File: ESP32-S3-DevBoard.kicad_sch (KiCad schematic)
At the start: 27 parts, among them J1 USB_C_Receptacle_USB2.0_14P, J2 Conn_01x22_Socket, J3 Conn_01x22_Socket, SW1 SW_Push, SW2 SW_Push, U1 ESP32-S3-WROOM-1, U2 AMS1117-3.3

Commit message: Add footprints
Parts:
- C1, C2, C3, C4, C5, C6, C7, C8, C9: footprint (none) -> Capacitor_SMD:C_0603_1608Metric_Pad1.08x0.95mm_HandSolder
- D1: footprint (none) -> LED_SMD:LED_0603_1608Metric_Pad1.05x0.95mm_HandSolder
- D2: footprint Diode_THT:D_DO-41_SOD81_P10.16mm_Horizontal -> Diode_SMD:D_SOD-123
- J1: footprint (none) -> Connector_USB:USB_C_Receptacle_GCT_USB4125-xx-x_6P_TopMnt_Horizontal
- J2, J3: footprint (none) -> Connector_PinSocket_2.54mm:PinSocket_1x22_P2.54mm_Vertical
- R1, R2, R3, R4, R5, R6: footprint (none) -> Resistor_SMD:R_0603_1608Metric_Pad0.98x0.95mm_HandSolder
- SW1, SW2: footprint (none) -> Button_Switch_SMD:SW_SPST_PTS810
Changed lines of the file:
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@@
 			)
 		)
-		(property "Footprint" ""
+		(property "Footprint" "Capacitor_SMD:C_0603_1608Metric_Pad1.08x0.95mm_HandSolder"
 			(at 157.7848 91.44 0)
 			(effects
@@
 			)
 		)
-		(property "Footprint" ""
+		(property "Footprint" "Capacitor_SMD:C_0603_1608Metric_Pad1.08x0.95mm_HandSolder"
 			(at 32.7152 40.64 0)
 			(effects
@@
 			)
 		)
-		(property "Footprint" ""
+		(property "Footprint" "Capacitor_SMD:C_0603_1608Metric_Pad1.08x0.95mm_HandSolder"
 			(at 136.8552 49.53 0)
 			(effects
@@
 			)
 		)
-		(property "Footprint" ""
+		(property "Footprint" "Connector_USB:USB_C_Receptacle_GCT_USB4125-xx-x_6P_TopMnt_Horizontal"
 			(at 111.76 140.97 0)
 			(effects
@@
 			)
 		)
-		(property "Footprint" ""
+		(property "Footprint" "Resistor_SMD:R_0603_1608Metric_Pad0.98x0.95mm_HandSolder"
 			(at 130.81 129.032 90)
 			(effects
@@
 			)
 		)
-		(property "Footprint" ""
+		(property "Footprint" "Capacitor_SMD:C_0603_1608Metric_Pad1.08x0.95mm_HandSolder"
 			(at 163.5252 149.86 0)
 			(effects
@@
 			)
 		)
-		(property "Footprint" ""
+		(property "Footprint" "LED_SMD:LED_0603_1608Metric_Pad1.05x0.95mm_HandSolder"
 			(at 176.53 87.63 0)
 			(effects
@@
 			)
 		)
-		(property "Footprint" ""
+		(property "Footprint" "Button_Switch_SMD:SW_SPST_PTS810"
 			(at 128.27 35.56 0)
 			(effects
@@
 			)
 		)
-		(property "Footprint" ""
+		(property "Footprint" "Connector_PinSocket_2.54mm:PinSocket_1x22_P2.54mm_Vertical"
 			(at 59.69 144.78 0)
 			(effects
@@
 			)
 		)
-		(property "Footprint" ""
+		(property "Footprint" "Capacitor_SMD:C_0603_1608Metric_Pad1.08x0.95mm_HandSolder"
 			(at 124.7648 91.44 0)
 			(effects
@@
 			)
 		)
-		(property "Footprint" ""
+		(property "Footprint" "Button_Switch_SMD:SW_SPST_PTS810"
 			(at 168.91 35.56 0)
 			(effects
@@
 			)
 		)
-		(property "Footprint" ""
+		(property "Footprint" "Capacitor_SMD:C_0603_1608Metric_Pad1.08x0.95mm_HandSolder"
 			(at 35.8648 40.64 0)
 			(effects
@@
 			)
 		)
-		(property "Footprint" ""
+		(property "Footprint" "Resistor_SMD:R_0603_1608Metric_Pad0.98x0.95mm_HandSolder"
 			(at 41.91 33.528 90)
 			(effects
@@
 			)
 		)
-		(property "Footprint" ""
+		(property "Footprint" "Resistor_SMD:R_0603_1608Metric_Pad0.98x0.95mm_HandSolder"
 			(at 137.922 35.56 90)
 			(effects
@@
 			)
 		)
-		(property "Footprint" ""
+		(property "Footprint" "Capacitor_SMD:C_0603_1608Metric_Pad1.08x0.95mm_HandSolder"
 			(at 131.7752 91.44 0)
 			(effects
@@
 			)
 		)
-		(property "Footprint" ""
+		(property "Footprint" "Capacitor_SMD:C_0603_1608Metric_Pad1.08x0.95mm_HandSolder"
 			(at 177.4952 49.53 0)
 			(effects
@@
 			)
 		)
-		(property "Footprint" ""
+		(property "Footprint" "Connector_PinSocket_2.54mm:PinSocket_1x22_P2.54mm_Vertical"
 			(at 49.53 144.78 0)
 			(effects
@@
 			)
 		)
-		(property "Footprint" ""
+		(property "Footprint" "Resistor_SMD:R_0603_1608Metric_Pad0.98x0.95mm_HandSolder"
 			(at 170.18 83.058 90)
 			(effects
@@
 			)
 		)
-		(property "Footprint" "Diode_THT:D_DO-41_SOD81_P10.16mm_Horizontal"
+		(property "Footprint" "Diode_SMD:D_SOD-123"
 			(at 154.94 121.285 0)
 			(effects
@@
 			)
 		)
-		(property "Footprint" ""
+		(property "Footprint" "Resistor_SMD:R_0603_1608Metric_Pad0.98x0.95mm_HandSolder"
 			(at 130.81 131.572 90)
 			(effects
@@
 			)
 		)
-		(property "Footprint" ""
+		(property "Footprint" "Capacitor_SMD:C_0603_1608Metric_Pad1.08x0.95mm_HandSolder"
 			(at 164.7952 91.44 0)
 			(effects
@@
 			)
 		)
-		(property "Footprint" ""
+		(property "Footprint" "Resistor_SMD:R_0603_1608Metric_Pad0.98x0.95mm_HandSolder"
 			(at 178.562 35.56 90)
 			(effects

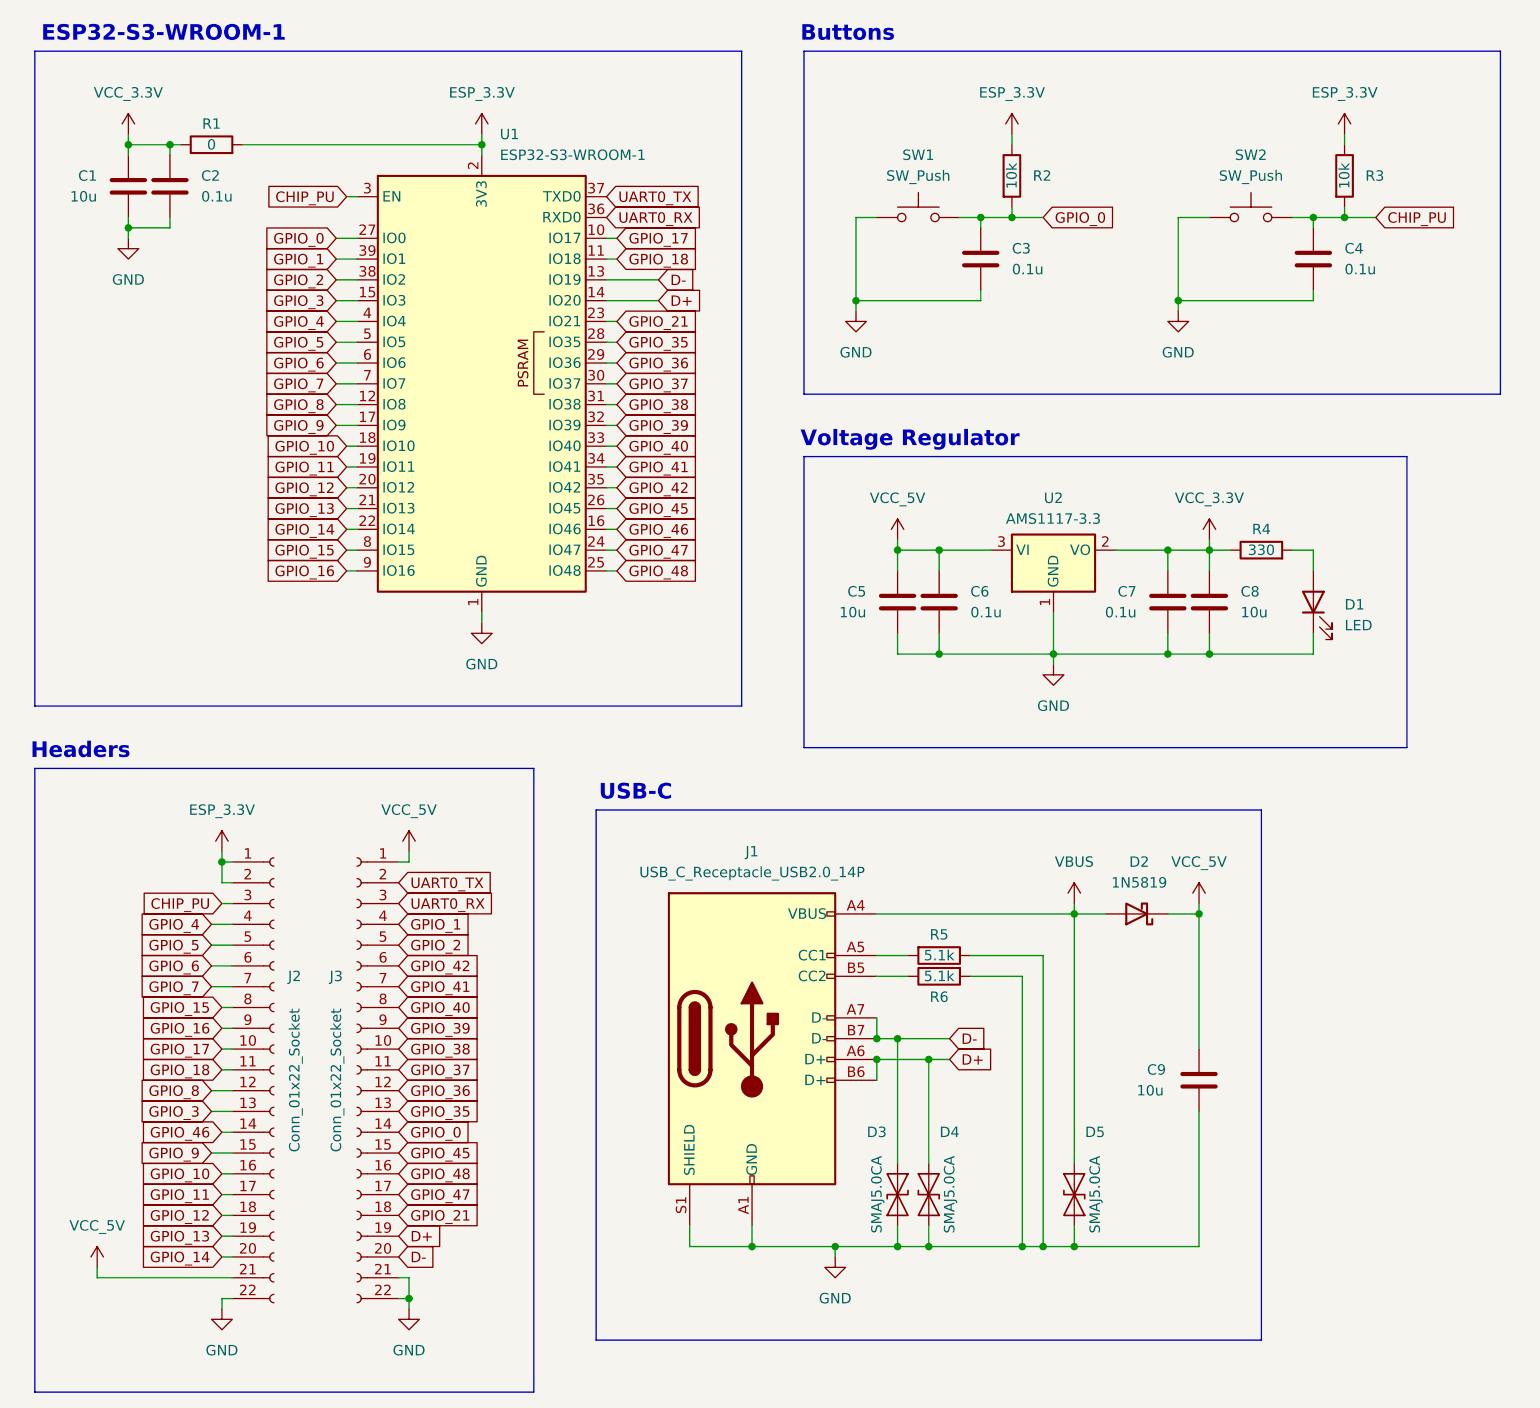
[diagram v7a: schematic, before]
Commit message: Route GPIOs and buttons
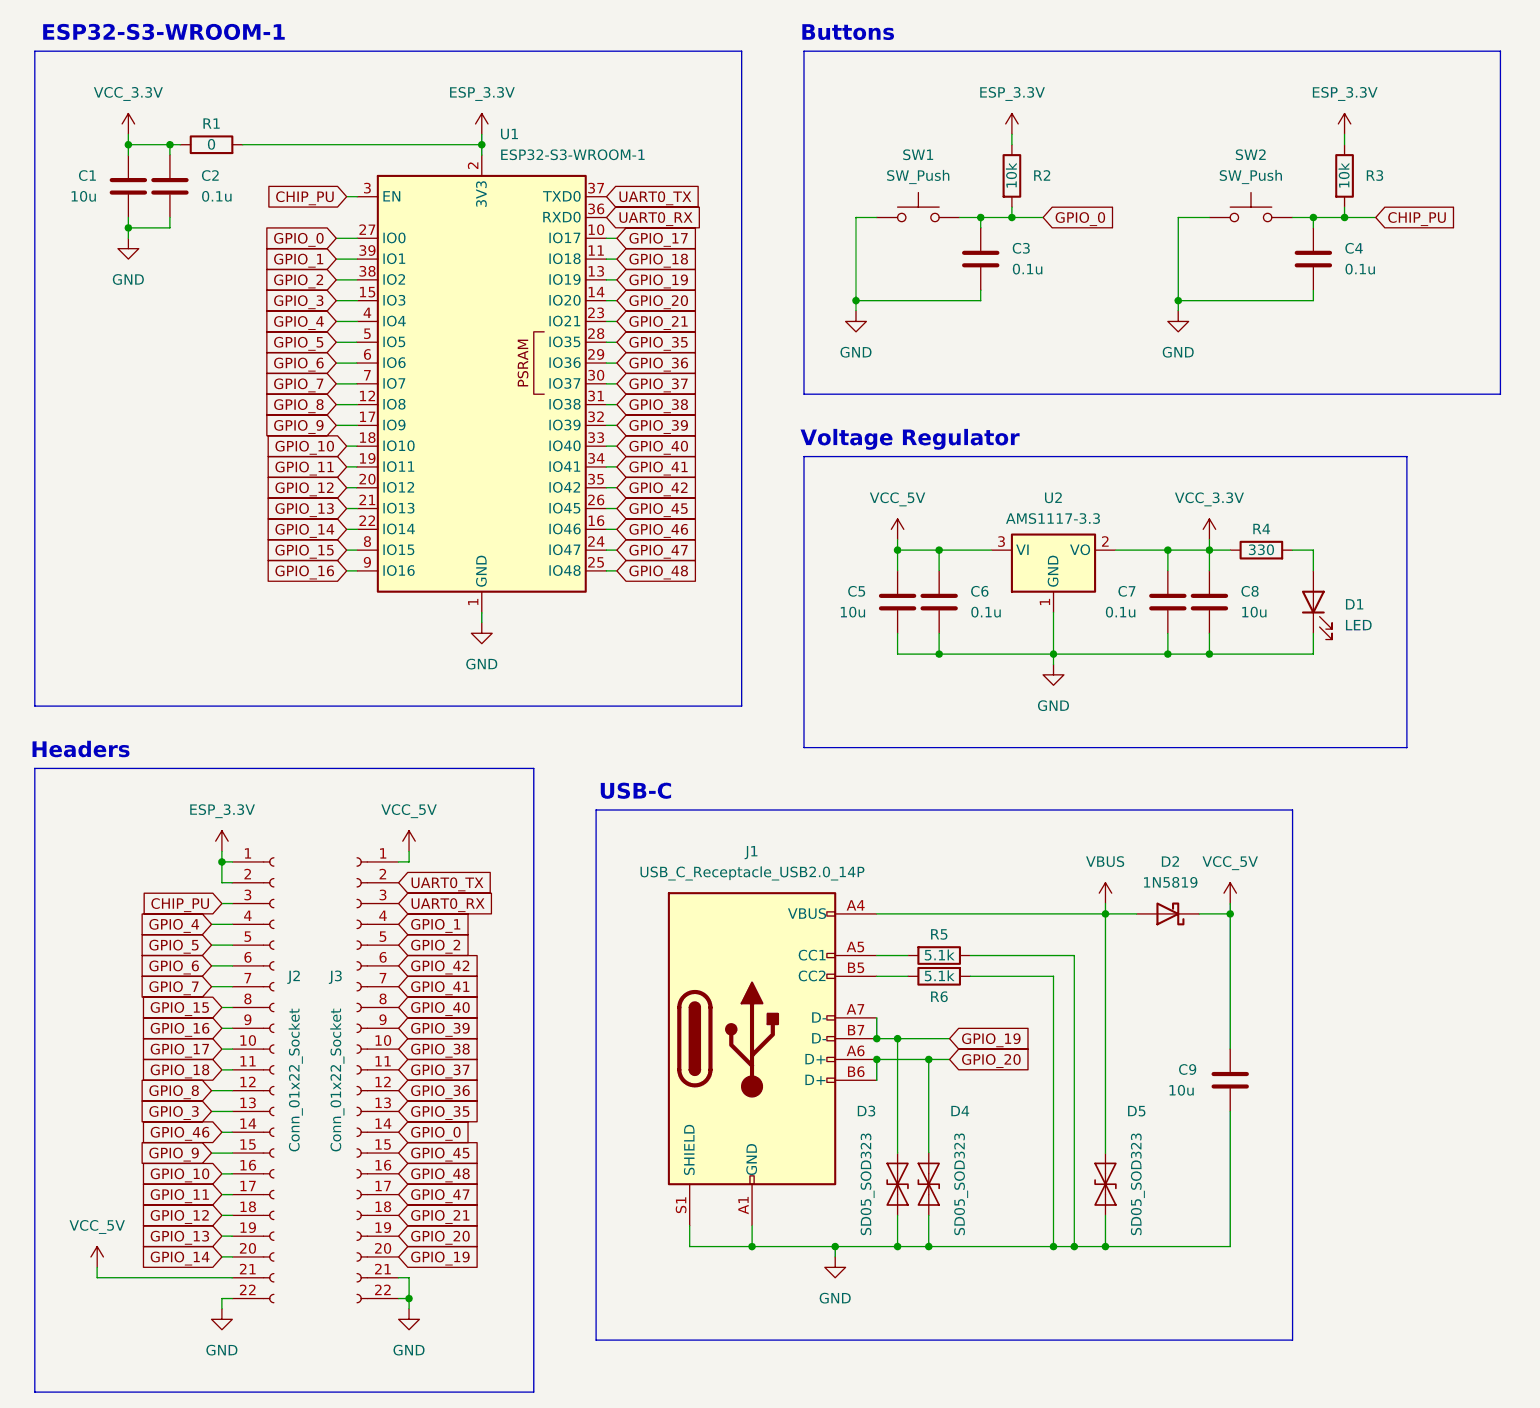
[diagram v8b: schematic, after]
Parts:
- removed D3, D4, D5: SMAJ5.0CA, Diode_SMD:D_SMA, symbol Diode:SMAJ5.0CA
- added D3, D4, D5: SD05_SOD323, Diode_SMD:D_SOD-323, symbol Diode:SD05_SOD323
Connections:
- net GND: now also D3.1 (A1), D4.2 (A2), D5.1 (A1)
- net VBUS: now also D5.2 (A2)
- net D+ renamed GPIO_20
- net GPIO_20: now also D4.1 (A1)
- net D- renamed GPIO_19
- net GPIO_19: now also D3.2 (A2)
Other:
- moved on the sheet: C9, D2
